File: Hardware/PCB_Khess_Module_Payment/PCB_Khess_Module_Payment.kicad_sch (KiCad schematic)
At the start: 53 parts, among them J1 Conn_02x20_Odd_Even, J2 Conn_01x02, J3 Conn_01x08, J4 Conn_01x04, J5 USB_C_Receptacle_USB2.0, J6 Conn_01x08, Q1 RE1C002UNTCL, U1 FSV330AF, U2 FSV330AF, U3 171013801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

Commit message: Add files via upload
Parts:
- C1, C3: footprint Capacitor_SMD:C_0805_2012Metric -> Capacitor_SMD:C_0603_1608Metric_Pad1.08x0.95mm_HandSolder
- C2, C8: footprint Capacitor_SMD:C_0402_1005Metric -> Capacitor_SMD:C_0603_1608Metric_Pad1.08x0.95mm_HandSolder
- C9: footprint (none) -> Capacitor_SMD:C_0603_1608Metric_Pad1.08x0.95mm_HandSolder
- L1: footprint (none) -> Inductor_SMD:L_0603_1608Metric_Pad1.05x0.95mm_HandSolder
- Q1: footprint (none) -> Package_TO_SOT_SMD:SOT-416
- R1, R12, R13, R14, R15, R17, R18, R19, R20, R4, R5, R6, R7: footprint Resistor_SMD:R_0402_1005Metric -> Resistor_SMD:R_0603_1608Metric_Pad0.98x0.95mm_HandSolder
- R16, R8, R9: footprint (none) -> Resistor_SMD:R_0603_1608Metric_Pad0.98x0.95mm_HandSolder
- U1, U2: footprint Schuttky:DO-214AD_ONS -> Diode_SMD:D_SOD-123
- U3: footprint Wurth_regulator_171013801:Wurth_171013801 -> Package_DFN_QFN:QFN-16-1EP_3x3mm_P0.5mm_EP1.9x1.9mm
- U4: footprint TP5100:QFN65P400X400X90-17N -> Package_DFN_QFN:QFN-16-1EP_4x4mm_P0.5mm_EP2.45x2.45mm
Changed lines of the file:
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@@
 			)
 		)
-		(property "Footprint" ""
+		(property "Footprint" "Resistor_SMD:R_0603_1608Metric_Pad0.98x0.95mm_HandSolder"
 			(at 143.51 138.43 0)
 			(effects
@@
 			)
 		)
-		(property "Footprint" ""
+		(property "Footprint" "Capacitor_SMD:C_0603_1608Metric_Pad1.08x0.95mm_HandSolder"
 			(at 210.82 83.82 0)
 			(effects
@@
 			)
 		)
-		(property "Footprint" "Resistor_SMD:R_0402_1005Metric"
+		(property "Footprint" "Resistor_SMD:R_0603_1608Metric_Pad0.98x0.95mm_HandSolder"
 			(at 66.802 153.67 90)
 			(effects
@@
 			)
 		)
-		(property "Footprint" "TP5100:QFN65P400X400X90-17N"
+		(property "Footprint" "Package_DFN_QFN:QFN-16-1EP_4x4mm_P0.5mm_EP2.45x2.45mm"
 			(at 232.41 76.2 0)
 			(effects
@@
 			)
 		)
-		(property "Footprint" "Schuttky:DO-214AD_ONS"
+		(property "Footprint" "Diode_SMD:D_SOD-123"
 			(at 45.72 189.23 0)
 			(effects
@@
 			)
 		)
-		(property "Footprint" "Resistor_SMD:R_0402_1005Metric"
+		(property "Footprint" "Resistor_SMD:R_0603_1608Metric_Pad0.98x0.95mm_HandSolder"
 			(at 228.6 127.508 90)
 			(effects
@@
 			)
 		)
-		(property "Footprint" ""
+		(property "Footprint" "Resistor_SMD:R_0603_1608Metric_Pad0.98x0.95mm_HandSolder"
 			(at 212.09 68.58 0)
 			(effects
@@
 			)
 		)
-		(property "Footprint" "Capacitor_SMD:C_0805_2012Metric"
+		(property "Footprint" "Capacitor_SMD:C_0603_1608Metric_Pad1.08x0.95mm_HandSolder"
 			(at 27.6352 149.86 0)
 			(effects
@@
 			)
 		)
-		(property "Footprint" ""
+		(property "Footprint" "Inductor_SMD:L_0603_1608Metric_Pad1.05x0.95mm_HandSolder"
 			(at 255.27 63.5 0)
 			(effects
@@
 			)
 		)
-		(property "Footprint" "Capacitor_SMD:C_0402_1005Metric"
+		(property "Footprint" "Capacitor_SMD:C_0603_1608Metric_Pad1.08x0.95mm_HandSolder"
 			(at 166.37 173.99 0)
 			(effects
@@
 			)
 		)
-		(property "Footprint" "Resistor_SMD:R_0402_1005Metric"
+		(property "Footprint" "Resistor_SMD:R_0603_1608Metric_Pad0.98x0.95mm_HandSolder"
 			(at 66.802 143.51 90)
 			(effects
@@
 			)
 		)
-		(property "Footprint" "Resistor_SMD:R_0402_1005Metric"
+		(property "Footprint" "Resistor_SMD:R_0603_1608Metric_Pad0.98x0.95mm_HandSolder"
 			(at 157.48 179.07 0)
 			(effects
@@
 			)
 		)
-		(property "Footprint" "Resistor_SMD:R_0402_1005Metric"
+		(property "Footprint" "Resistor_SMD:R_0603_1608Metric_Pad0.98x0.95mm_HandSolder"
 			(at 205.74 36.068 90)
 			(effects
@@
 			)
 		)
-		(property "Footprint" "Resistor_SMD:R_0402_1005Metric"
+		(property "Footprint" "Resistor_SMD:R_0603_1608Metric_Pad0.98x0.95mm_HandSolder"
 			(at 29.972 153.67 90)
 			(effects
@@
 			)
 		)
-		(property "Footprint" ""
+		(property "Footprint" "Resistor_SMD:R_0603_1608Metric_Pad0.98x0.95mm_HandSolder"
 			(at 146.05 133.35 0)
 			(effects
@@
 			)
 		)
-		(property "Footprint" "Capacitor_SMD:C_0402_1005Metric"
+		(property "Footprint" "Capacitor_SMD:C_0603_1608Metric_Pad1.08x0.95mm_HandSolder"
 			(at 37.7952 162.56 0)
 			(effects
@@
 			)
 		)
-		(property "Footprint" ""
+		(property "Footprint" "Package_TO_SOT_SMD:SOT-416"
 			(at 156.21 135.89 0)
 			(effects
@@
 			)
 		)
-		(property "Footprint" "Resistor_SMD:R_0402_1005Metric"
+		(property "Footprint" "Resistor_SMD:R_0603_1608Metric_Pad0.98x0.95mm_HandSolder"
 			(at 233.68 27.178 90)
 			(effects
@@
 			)
 		)
-		(property "Footprint" "Resistor_SMD:R_0402_1005Metric"
+		(property "Footprint" "Resistor_SMD:R_0603_1608Metric_Pad0.98x0.95mm_HandSolder"
 			(at 205.74 27.178 90)
 			(effects
@@
 			)
 		)
-		(property "Footprint" "Resistor_SMD:R_0402_1005Metric"
+		(property "Footprint" "Resistor_SMD:R_0603_1608Metric_Pad0.98x0.95mm_HandSolder"
 			(at 228.6 122.428 90)
 			(effects
@@
 			)
 		)
-		(property "Footprint" "Resistor_SMD:R_0402_1005Metric"
+		(property "Footprint" "Resistor_SMD:R_0603_1608Metric_Pad0.98x0.95mm_HandSolder"
 			(at 118.11 166.37 0)
 			(effects
@@
 			)
 		)
-		(property "Footprint" "Capacitor_SMD:C_0805_2012Metric"
+		(property "Footprint" "Capacitor_SMD:C_0603_1608Metric_Pad1.08x0.95mm_HandSolder"
 			(at 82.2452 152.4 0)
 			(effects
@@
 			)
 		)
-		(property "Footprint" "Resistor_SMD:R_0402_1005Metric"
+		(property "Footprint" "Resistor_SMD:R_0603_1608Metric_Pad0.98x0.95mm_HandSolder"
 			(at 157.48 168.91 0)
 			(effects
@@
 			)
 		)
-		(property "Footprint" "Resistor_SMD:R_0402_1005Metric"
+		(property "Footprint" "Resistor_SMD:R_0603_1608Metric_Pad0.98x0.95mm_HandSolder"
 			(at 233.68 36.068 90)
 			(effects
@@
 			)
 		)
-		(property "Footprint" "Wurth_regulator_171013801:Wurth_171013801"
+		(property "Footprint" "Package_DFN_QFN:QFN-16-1EP_3x3mm_P0.5mm_EP1.9x1.9mm"
 			(at 49.53 132.08 0)
 			(effects
@@
 			)
 		)
-		(property "Footprint" "Resistor_SMD:R_0402_1005Metric"
+		(property "Footprint" "Resistor_SMD:R_0603_1608Metric_Pad0.98x0.95mm_HandSolder"
 			(at 93.98 165.1 0)
 			(effects
@@
 			)
 		)
-		(property "Footprint" "Schuttky:DO-214AD_ONS"
+		(property "Footprint" "Diode_SMD:D_SOD-123"
 			(at 45.72 177.8 0)
 			(effects

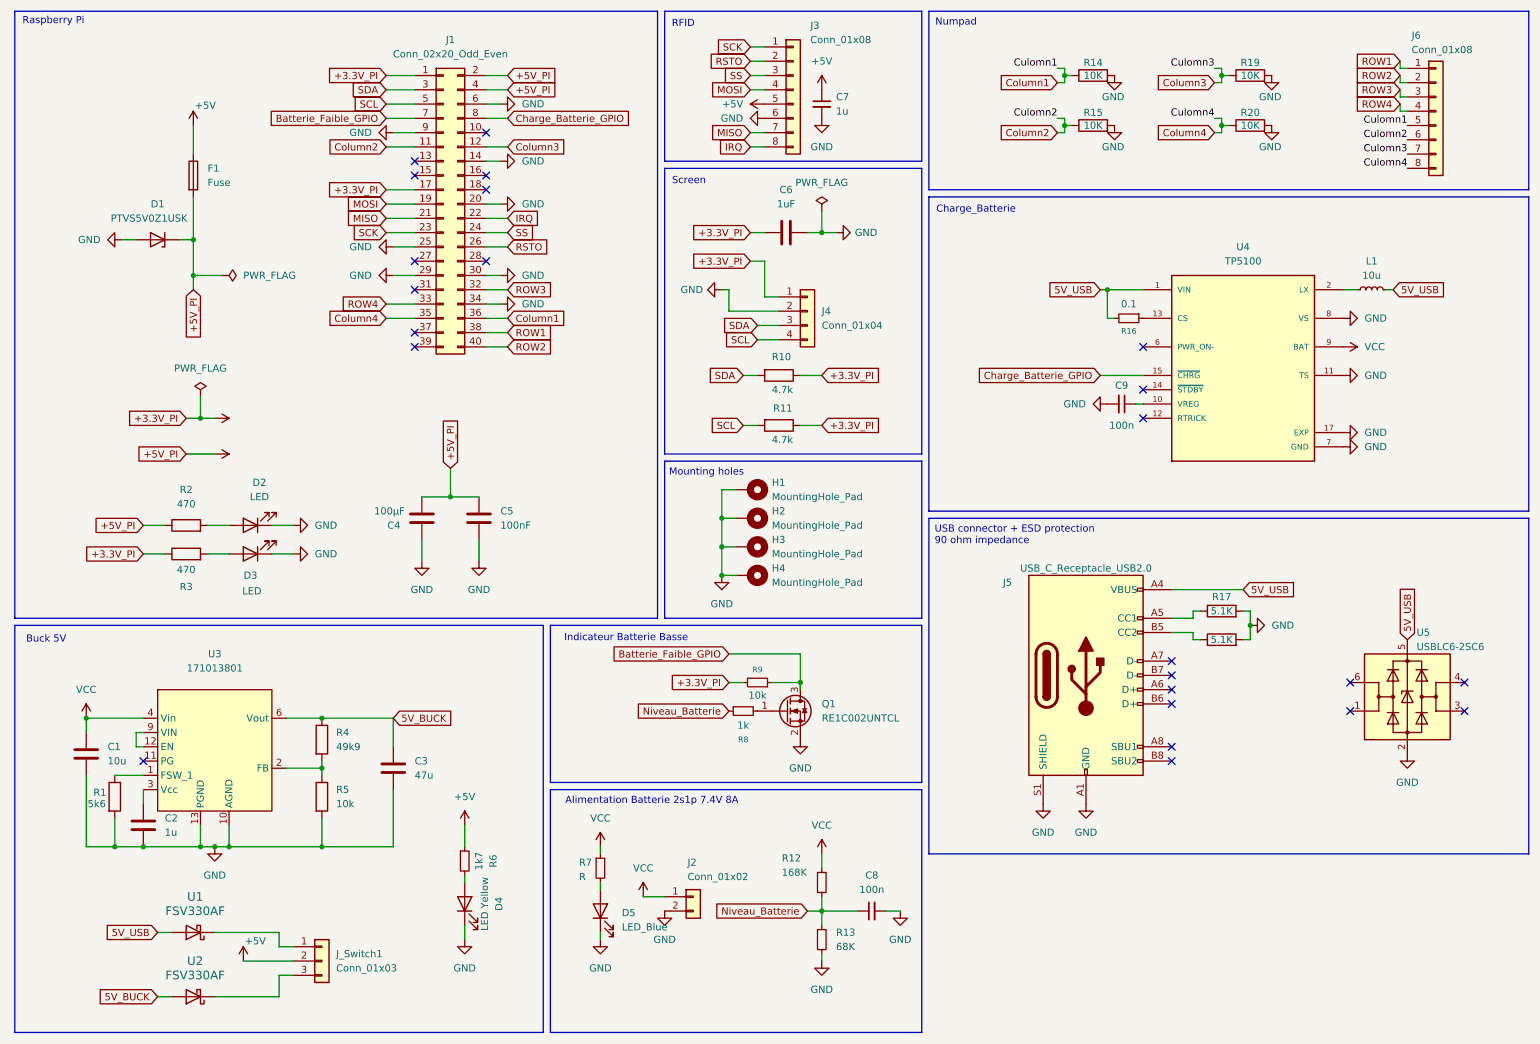
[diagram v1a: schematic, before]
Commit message: fix: update module payment schematic
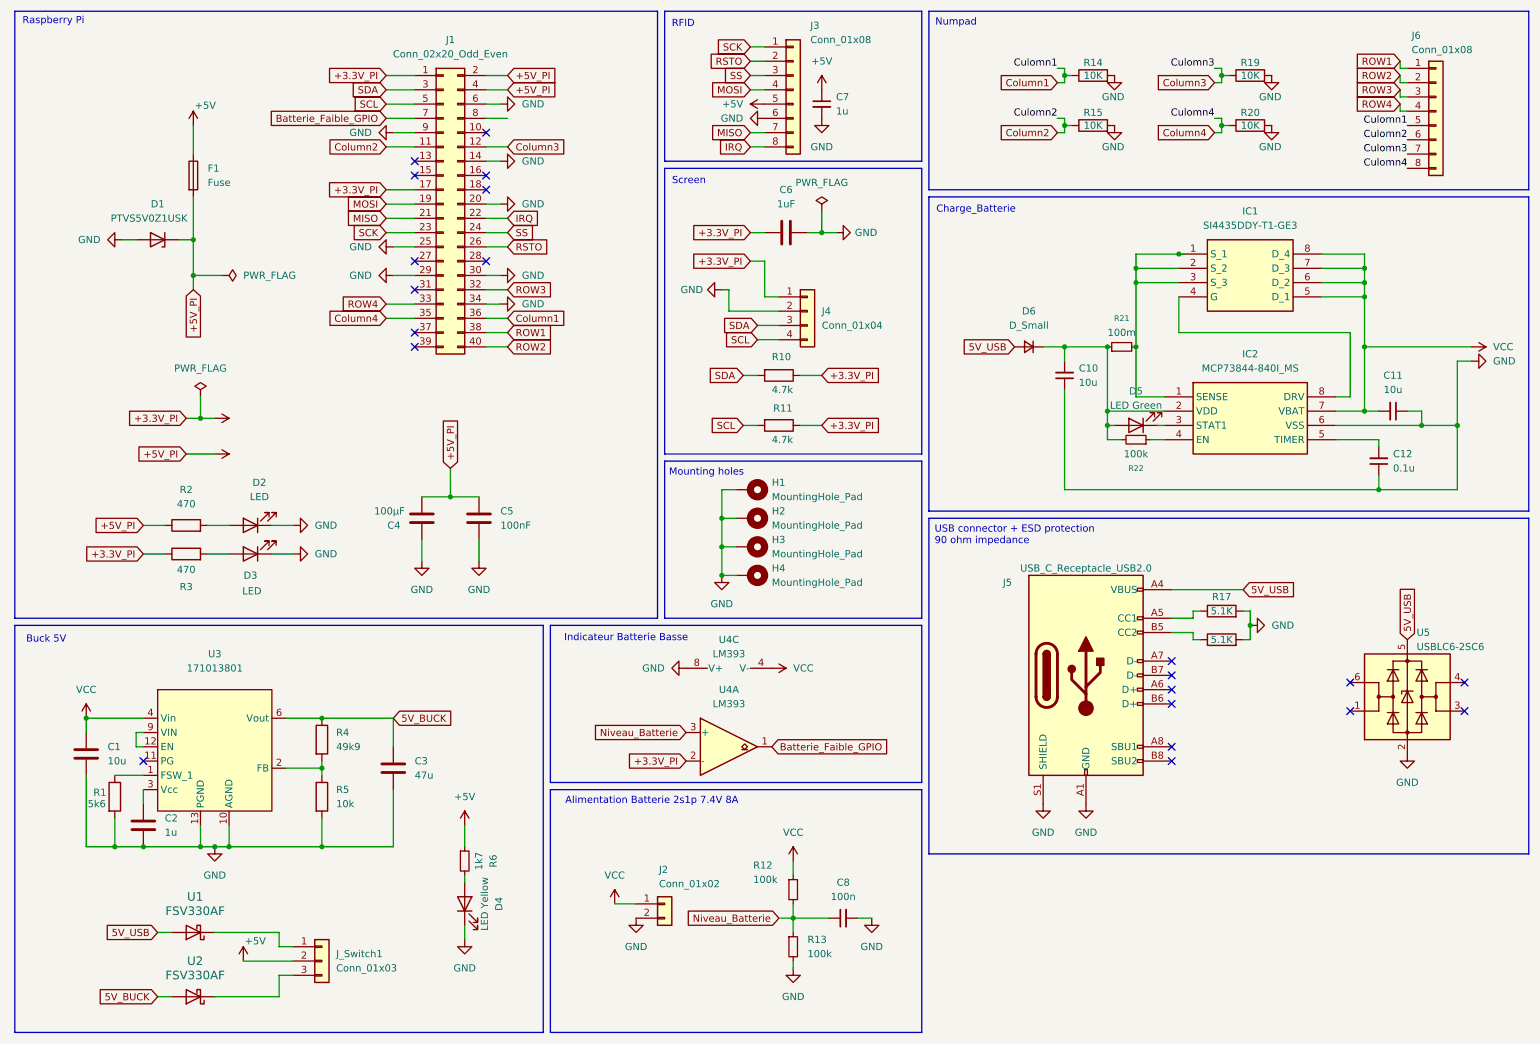
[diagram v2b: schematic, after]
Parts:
- removed C9: 100n, Capacitor_SMD:C_0603_1608Metric_Pad1.08x0.95mm_HandSolder, symbol Device:C_Small
- removed L1: 10u, Inductor_SMD:L_0603_1608Metric_Pad1.05x0.95mm_HandSolder, symbol Device:L_Small
- removed Q1: RE1C002UNTCL, Package_TO_SOT_SMD:SOT-416, symbol Transistor_FET:Q_NMOS_GSD
- removed R16: 0.1, Resistor_SMD:R_0603_1608Metric_Pad0.98x0.95mm_HandSolder, symbol Device:R_Small
- removed R7: R, Resistor_SMD:R_0603_1608Metric_Pad0.98x0.95mm_HandSolder, symbol Device:R_Small
- removed R8: 1k, Resistor_SMD:R_0603_1608Metric_Pad0.98x0.95mm_HandSolder, symbol Device:R_Small
- removed R9: 10k, Resistor_SMD:R_0603_1608Metric_Pad0.98x0.95mm_HandSolder, symbol Device:R_Small
- removed U4: TP5100, Package_DFN_QFN:QFN-16-1EP_4x4mm_P0.5mm_EP2.45x2.45mm, symbol TP5100:TP5100
- added C10, C11: 10u, symbol Device:C_Small
- added C12: 0.1u, symbol Device:C_Small
- added D6: D_Small, symbol Device:D_Small
- added IC1: SI4435DDY-T1-GE3, SOIC127P600X175-8N, symbol SI4435DDY-T1-GE3:SI4435DDY-T1-GE3
- added IC2: MCP73844-840I_MS, SOP65P490X110-8N, symbol MCP73844-840I_MS:MCP73844-840I_MS
- added R21: 100m, symbol Device:R_Small
- added R22: 100k, symbol Device:R_Small
- added U4: LM393, symbol Comparator:LM393
- D5: value LED_Blue -> LED Green; MPN (none) -> 150060YS55040
- R12: value 168K -> 100k
- R13: value 68K -> 100k
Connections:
- net +3.3V: now also U4.2 (-)
- net 5V_USB: now also D6.2 (A)
- net Batterie_Faible_GPIO: now also U4.1
- net GND: now also C10.1, C11.1, C12.1, IC2.6 (VSS), U4.8 (V+); no longer D5.1 (K)
- net Niveau_Batterie: now also U4.3 (+)
- net VCC: now also C11.2, IC1.5 (D_1), IC1.6 (D_2), IC1.7 (D_3), IC1.8 (D_4), IC2.7 (VBAT), U4.4 (V-)
- net at D5.2 (A): now also C10.2, D6.1 (K), IC2.2 (VDD), R21.1, R22.2
- net Charge_Batterie_GPIO: no longer names the net of J1.8 (Pin_8)
- new net: IC1.1 (S_1), IC1.2 (S_2), IC1.3 (S_3), IC2.1 (SENSE), R21.2
- new net: IC2.4 (EN), R22.1
- new net: IC1.4 (G), IC2.8 (DRV)
- new net: D5.1 (K), IC2.3 (STAT1)
- new net: C12.2, IC2.5 (TIMER)
- no-connect marks 24 -> 21
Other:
- moved on the sheet: C8, J2, R12, R13

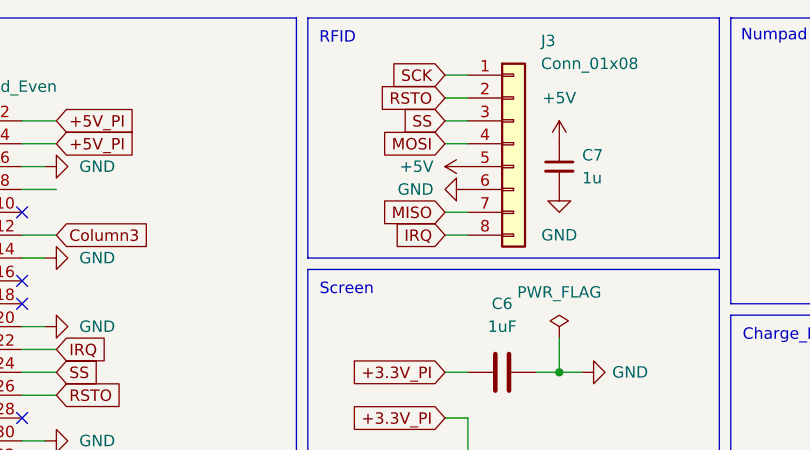
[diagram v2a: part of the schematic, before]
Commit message: fix: update connector rfid module payment
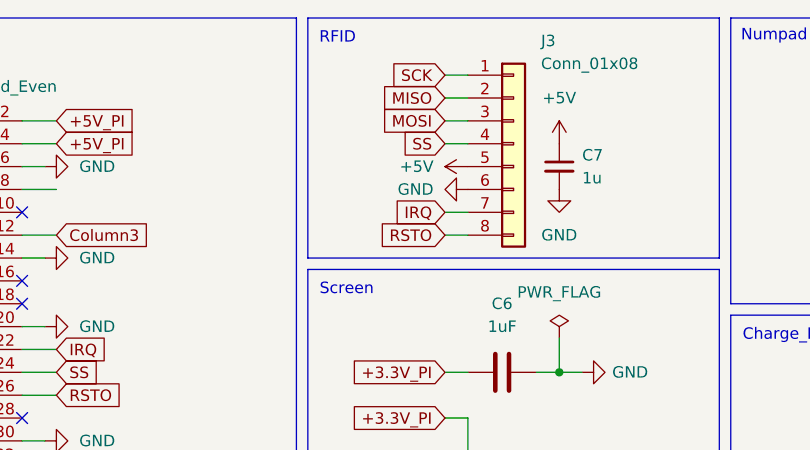
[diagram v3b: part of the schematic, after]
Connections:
- net IRQ: now also J3.7 (Pin_7); no longer J3.8 (Pin_8)
- net MISO: now also J3.2 (Pin_2); no longer J3.7 (Pin_7)
- net MOSI: now also J3.3 (Pin_3); no longer J3.4 (Pin_4)
- net RSTO: now also J3.8 (Pin_8); no longer J3.2 (Pin_2)
- net SS: now also J3.4 (Pin_4); no longer J3.3 (Pin_3)
